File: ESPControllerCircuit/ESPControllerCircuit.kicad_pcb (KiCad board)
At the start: 2 copper layers, 85 x 30 mm, 25 parts, among them J1 Input, J2 Input, J3 Input, J4 Input, J5 Optional, U1 WeMos_mini, U2 HMHA2801, U3 PCF8574AT/3

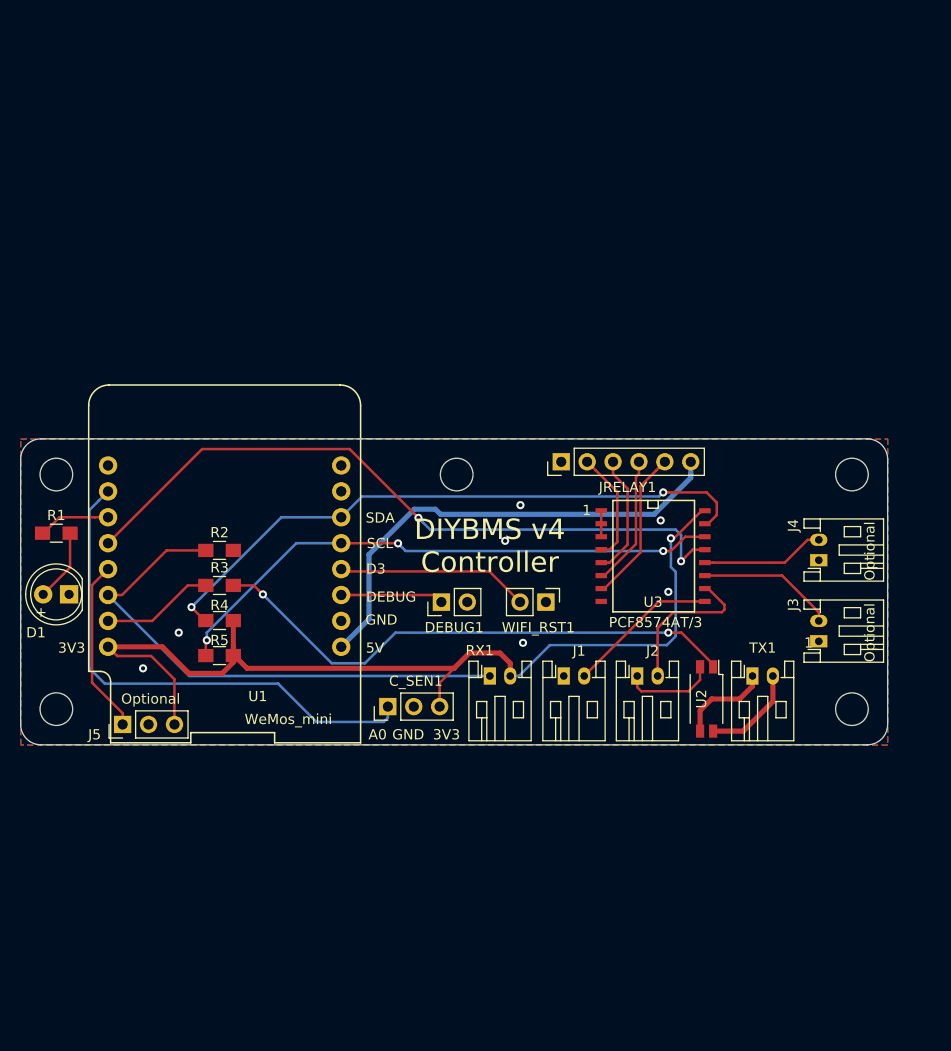
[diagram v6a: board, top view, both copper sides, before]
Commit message: Reduced board by 10mm in width to 75mm
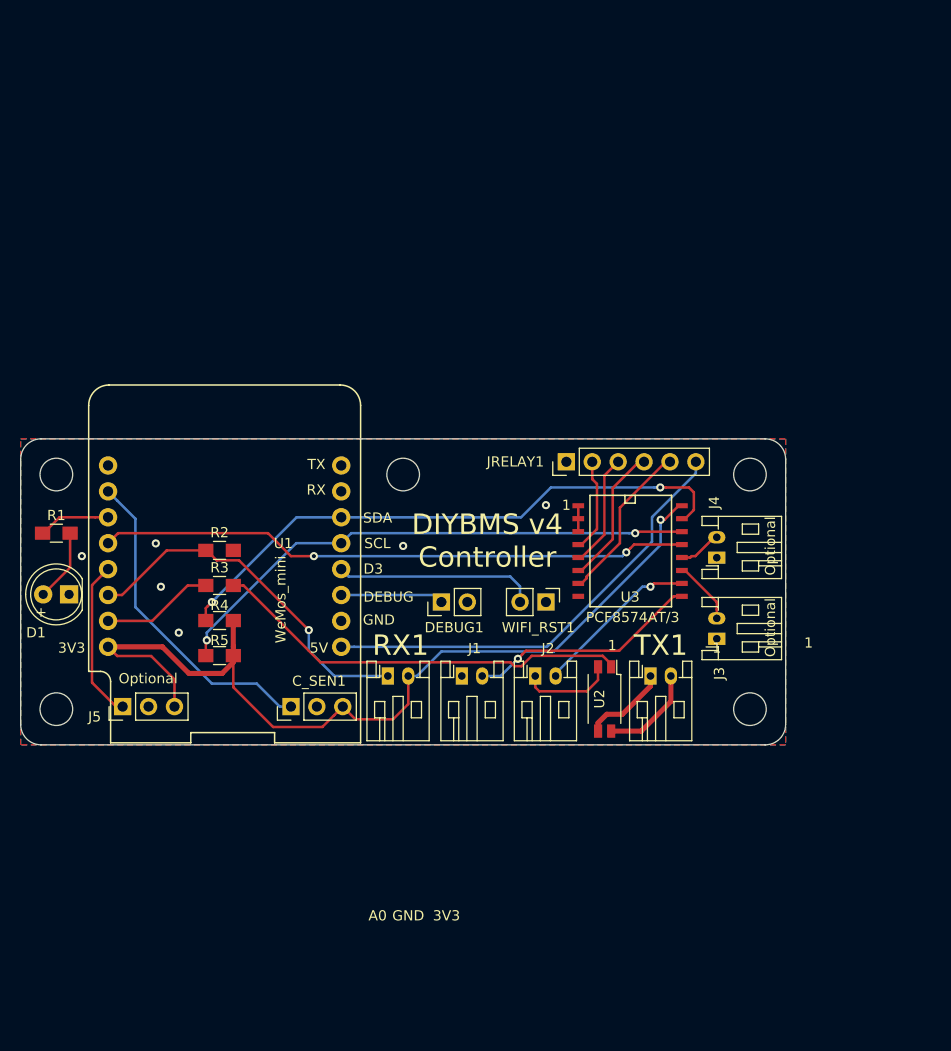
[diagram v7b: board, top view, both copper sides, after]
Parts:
- removed the REF** at (154.0, 128.5)
- removed the REF** at (154.0, 105.5)
- added REF**: MountingHole_3.2mm_M3, Mounting_Holes:MountingHole_3.2mm_M3, F.Cu at (144.0, 128.5)
- added REF**: MountingHole_3.2mm_M3, Mounting_Holes:MountingHole_3.2mm_M3, F.Cu at (144.0, 105.5)
- moved J3 10.0 mm to (140.8, 121.6)
- moved J4 10.0 mm to (140.8, 113.7)
- moved J1 10.0 mm to (115.8, 125.2)
- moved RX1 10.0 mm to (108.5, 125.2)
- moved TX1 10.0 mm to (134.2, 125.2)
- moved U2 10.0 mm to (129.8, 127.5)
- moved J2 10.00 mm to (123.0, 125.2)
- moved C_SEN1 9.50 mm to (99.0, 128.2)
- moved REF** 5.25 mm to (110.0, 105.5)
- moved U3 2.30 mm to (132.2, 113.0)
- moved J5 1.75 mm to (82.5, 128.2)
- moved JRELAY1 0.50 mm to (126.0, 104.2)
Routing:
- net Net-(C_SEN1-Pad1): track 50.8 -> 31.7 mm
- net Net-(R2-Pad2): track 52.1 -> 35.5 mm, vias 0 -> 1
- net Net-(R3-Pad1): track 53.0 -> 41.3 mm, vias 2 -> 0
- net PCFINT: track 68.9 -> 58.1 mm
- net +3V3: track 98.7 -> 90.2 mm
- net Net-(J1-Pad2): track 14.9 -> 22.8 mm, vias 0 -> 1
- net Net-(J4-Pad2): track 12.1 -> 4.24 mm
- net Net-(J3-Pad2): track 13.5 -> 6.30 mm
- net SDA: track 61.3 -> 57.4 mm
- net SCL: track 55.7 -> 53.0 mm, vias 3 -> 2
- net +5V: track 46.8 -> 44.4 mm
- net Net-(JRELAY1-Pad2): track 11.0 -> 9.25 mm
- net Net-(J2-Pad2): track 15.1 -> 16.5 mm, vias 0 -> 1
- net Net-(J5-Pad1): track 17.1 -> 15.8 mm
- net Net-(JRELAY1-Pad4): track 12.9 -> 13.8 mm
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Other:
- board size 85 x 30 mm -> 75 x 30 mm
- board text added: "7 June 2019"
- board text added: "RX"
- board text added: "TX"
- board text removed: "22 May 2019"
